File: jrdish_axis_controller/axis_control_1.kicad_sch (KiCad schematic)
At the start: 31 parts, among them CN1 KF2EDGR-2.54-9P, CN2 KF2EDGR-2.54-6P

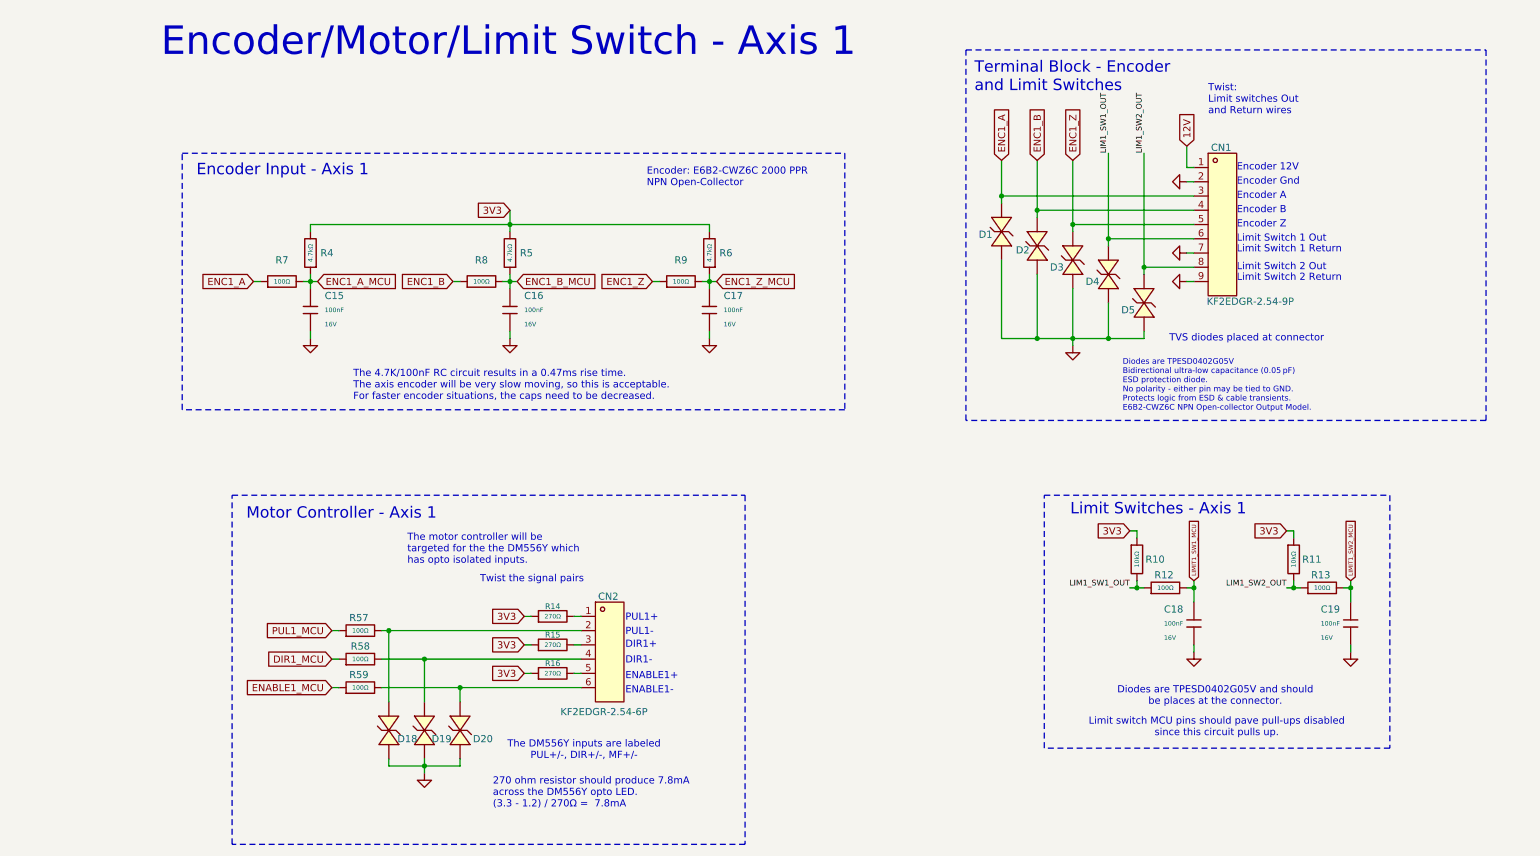
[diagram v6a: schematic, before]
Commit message: Limit switches with mosfets
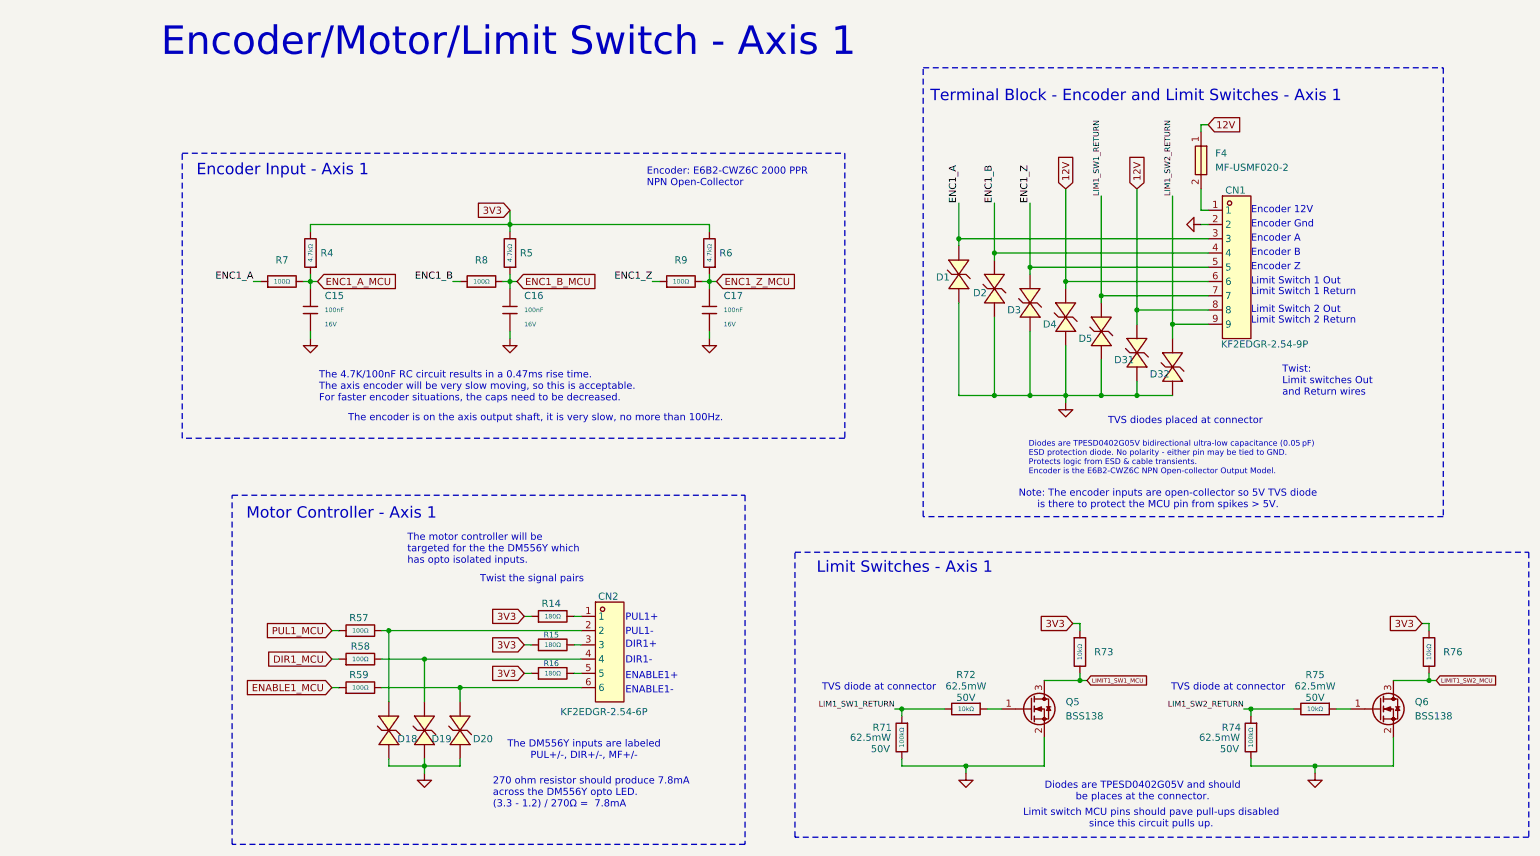
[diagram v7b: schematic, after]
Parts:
- removed C18, C19: 100nF, PCM_JLCPCB:C_0402, symbol PCM_JLCPCB-Capacitors:0402,100nF
- removed R10, R11: 10kΩ, PCM_JLCPCB:R_0402, symbol PCM_JLCPCB-Resistors:0402,10kΩ
- removed R12, R13: 100Ω, PCM_JLCPCB:R_0402, symbol PCM_JLCPCB-Resistors:0402,100Ω
- removed R14, R15, R16: 270Ω, PCM_JLCPCB:R_0603, symbol PCM_JLCPCB-Resistors:0603,270Ω
- added D31, D32: TPESD0402G05V, MyParts:D0402-BI, symbol MyParts:TPESD0402G05V
- added F4: MF-USMF020-2, MyParts:F1210, symbol MyParts:MF-USMF020-2
- added Q5, Q6: BSS138, Package_TO_SOT_SMD:SOT-23, symbol Transistor_FET:BSS138
- added R14, R15, R16: 180Ω, PCM_JLCPCB:R_0603, symbol PCM_JLCPCB-Resistors:0603,180Ω
- added R71, R74: 100kΩ, PCM_JLCPCB:R_0402, symbol PCM_JLCPCB-Resistors:0402,100kΩ
- added R72, R73, R75, R76: 10kΩ, PCM_JLCPCB:R_0402, symbol PCM_JLCPCB-Resistors:0402,10kΩ
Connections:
- net LIM1_SW1_OUT is gone; now on net 12V: CN1.6, D4.1 (K)
- net 12V: now also CN1.8, D31.1 (K), F4.1; no longer CN1.1
- net 3V3: now also R14.1, R15.1, R16.1, R73.1, R76.1
- net LIMIT1_SW1_MCU: now also Q5.3 (D), R73.2
- net LIMIT1_SW2_MCU: now also Q6.3 (D), R76.2
- net at CN2.3: now also R15.2
- net GND: now reaches D1.2 (A), D2.2 (A), D3.2 (A), D4.2 (A), D5.2 (A)
- net GND: now also C15.2, C16.2, C17.2, CN1.2, D18.2 (A), D19.2 (A), D20.2 (A), D31.2 (A), D32.2 (A), Q5.2 (S), Q6.2 (S), R71.2, R74.2
- net at CN2.1: now also R14.2
- net LIM1_SW1_RETURN: now reaches CN1.7
- net LIM1_SW1_RETURN: now also D5.1 (K), R71.1, R72.2
- net LIM1_SW2_RETURN: now reaches CN1.9
- net LIM1_SW2_RETURN: now also D32.1 (K), R74.1, R75.2
- net at CN2.5: now also R16.2
- removed net LIM1_SW2_OUT: CN1.8, D5.1 (K)
- new net: CN1.1, F4.2
- new net: Q5.1 (G), R72.1
- new net: Q6.1 (G), R75.1
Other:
- note added: "Diodes are TPESD0402G05V bidirectional ultra-low capacitance (0.05 pF) ESD protection diode. No polarity - either pin may be tied to GND. Protects logic from ESD & cable transients. Encoder is the E6B2-CWZ6C NPN Open-collector Output Model."
- note added: "Note: The encoder inputs are open-collector so 5V TVS diode is there to protect the MCU pin from spikes > 5V."
- note added: "TVS diode at connector"
- note added: "Terminal Block - Encoder and Limit Switches - Axis 1"
- note added: "The encoder is on the axis output shaft, it is very slow, no more than 100Hz."
- note removed: "Diodes are TPESD0402G05V Bidirectional ultra-low capacitance (0.05 pF) ESD protection diode. No polarity - either pin may be tied to GND. Protects logic from ESD & cable transients. E6B2-CWZ6C NPN Open-collector Output Model."
- note removed: "Terminal Block - Encoder and Limit Switches"
- moved on the sheet: D1, D2, D3, D4, D5

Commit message: Refinements...
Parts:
- removed D31, D32, D4, D5: TPESD0402G05V, MyParts:D0402-BI, symbol MyParts:TPESD0402G05V
- added D31, D32, D4, D5: TPESD0402G15V, MyParts:D0402-BI, symbol MyParts:TPESD0402G15V
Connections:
- net 12V: now also D31.2, D4.2
- net GND: now also D31.1, D32.1, D4.1, D5.1
- net LIM1_SW1_RETURN: now also D5.2
- net LIM1_SW2_RETURN: now also D32.2
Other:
- note added: "Diodes are TPESD0402G05V and TPESD0402G15V bidirectional ultra-low capacitance (0.05 pF) ESD protection diode. No polarity - either pin may be tied to GND. Protects logic from ESD & cable transients. Encoder is the E6B2-CWZ6C NPN Open-collector Output Model."
- note added: "Diodes are TPESD0402G05V and should be placed at the connector."
- note removed: "Diodes are TPESD0402G05V and should be places at the connector."
- note removed: "Diodes are TPESD0402G05V bidirectional ultra-low capacitance (0.05 pF) ESD protection diode. No polarity - either pin may be tied to GND. Protects logic from ESD & cable transients. Encoder is the E6B2-CWZ6C NPN Open-collector Output Model."
